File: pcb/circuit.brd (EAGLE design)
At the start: 80 x 70 mm, 148 parts, among them IC1 MCP1612-ADJI/MS, IC2 MCP73833-AMI/UN-ND, IC3 WE-TVS, IC4 MCP3423, IC5 ATWINC1510-MR210PB1952-ND, IC6 MAX3378EEUD, IC7 RN4870, IC8 ATSAML22N18A, J1 22-05-7038-03, J2 22-05-7038-03, Q1 ECX-1210, T1 PMOS, T10 NMOSSOT323, T11 NMOSSOT323, T12 NMOSSOT323, T2 NMOSSOT323, T3 NMOSSOT323, T4 NMOSSOT323, T5 NMOSSOT323, T6 NMOSSOT323, T7 NMOSSOT323, T8 NMOSSOT323, T9 NMOSSOT323, X1 USB2-MICRO, X10 2.5MM-AUDIO-JACK-MONONO_DRILL, X11 2.5MM-AUDIO-JACK-MONONO_DRILL, X12 2.5MM-AUDIO-JACK-MONONO_DRILL, X13 2.5MM-AUDIO-JACK-MONONO_DRILL, X14 MOLEX_1MM_FPC, X15 IGRID-20, X2 B3S-1000, X4 2.5MM-AUDIO-JACK-MONODRILL, X5 2.5MM-AUDIO-JACK-MONODRILL, X6 2.5MM-AUDIO-JACK-MONODRILL, X7 2.5MM-AUDIO-JACK-MONODRILL, X8 2.5MM-AUDIO-JACK-MONODRILL, X9 2.5MM-AUDIO-JACK-MONONO_DRILL

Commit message: routed RN4970
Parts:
- moved R19 31.4 mm to (62.5, 21.8), turned to 90 degrees
- moved C21 31.1 mm to (51.5, 23.6), flipped to the top, turned to 270 degrees
- moved R18 29.6 mm to (60.5, 21.8), turned to 90 degrees
- moved JP6 18.7 mm to (63.1, 35.1), turned to 180 degrees
- moved JP3 17.7 mm to (56.4, 23.4)
- moved R57 14.3 mm to (14.6, 15.2), turned to 0 degrees
- moved JP1 13.9 mm to (60.0, 46.0)
- moved T12 13.6 mm to (14.6, 13.7), turned to 180 degrees
- moved JP7 12.1 mm to (73.0, 51.0)
- moved R23 9.09 mm to (20.3, 39.9)
- moved C27 1.00 mm to (25.1, 43.7)
- moved C30 1.00 mm to (25.1, 45.8)
- moved C32 1.00 mm to (25.1, 47.9)
- moved C34 0.85 mm to (9.34, 27.5)
- moved C13 0.67 mm to (29.2, 31.4), turned to 180 degrees
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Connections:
- net !PG!_TRANS: now also IC6.3; no longer IC6.2
- net BT_MODE: now also IC8.71; no longer IC8.67
- net BT_PAIRING_KEY: now also IC8.67; no longer IC8.71
- net BT_RSSI_IND: now also IC8.70; no longer IC8.68
- net BT_RX_IND: now also IC8.68; no longer IC8.70
- net CHARGER_!PG!: now also IC6.12; no longer IC6.13
- net CHARGER_STAT1: now also IC6.11; no longer IC6.12
- net CHARGER_STAT2: now also IC6.10; no longer IC6.11
- net CHARGER_VUSB_FIL: now also IC6.13; no longer IC6.10
- net OLED_D/C: now also IC8.43; no longer IC8.44
- net OLED_EN: now also IC8.44; no longer IC8.43
- net SENSOR_EN_2: now also IC8.22; no longer IC8.21
- net SENSOR_EN_3: now also IC8.20; no longer IC8.19
- net SENSOR_EN_7: now also IC8.21; no longer IC8.22
- net SENSOR_EN_8: now also IC8.19; no longer IC8.20
- net STAT1_TRANS: now also IC6.4; no longer IC6.3
- net STAT2_TRANS: now also IC6.5; no longer IC6.4
- net USB_CON_INT_TRANS: now also IC6.2; no longer IC6.5
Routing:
- net GND: track 246.0 -> 340.1 mm, vias 6 -> 16
- net BT_UART_TX: track 0.00 -> 71.8 mm, vias 0 -> 2
- net BT_UART_RX: track 0.00 -> 71.3 mm, vias 0 -> 2
- net BT_UART_RTS: track 0.00 -> 55.8 mm, vias 0 -> 4
- net BT_UART_CTS: track 0.00 -> 52.9 mm, vias 0 -> 2
- net !OLED_SPI_CS: track 0.00 -> 49.9 mm, vias 0 -> 1
- net SENSOR_IN_4: track 5.16 -> 51.6 mm, vias 0 -> 1
- net SENSOR_INT_9: track 0.00 -> 44.0 mm, vias 0 -> 2
- net BT_STATUS_1: track 0.00 -> 43.5 mm, vias 0 -> 3
- net SENSOR_IN_7: track 0.21 -> 43.6 mm, vias 0 -> 2
- net BT_STATUS_2: track 0.00 -> 43.0 mm, vias 0 -> 3
- net SENSOR_IN_6: track 5.38 -> 48.4 mm, vias 0 -> 2
- net BT_PAIRING_KEY: track 0.00 -> 42.6 mm, vias 0 -> 1
- net BT_RX_IND: track 0.00 -> 42.0 mm, vias 0 -> 1
- net OLED_SPI_MOSI: track 0.00 -> 41.5 mm
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
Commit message: started routing ATWINC
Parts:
- removed JP2: (no value), thermo:JP4
- added JP8: (no value), thermo:JP3
- moved JP5 58.0 mm to (9.30, 29.9), turned to 180 degrees
- moved R26 7.20 mm to (19.9, 46.0)
- moved R24 6.38 mm to (15.8, 46.0)
- moved R27 4.84 mm to (22.0, 46.0)
- moved JP1 4.06 mm to (56.1, 44.7)
- moved JP4 4.02 mm to (60.6, 38.9)
- moved R25 2.81 mm to (17.9, 46.0)
- moved L5 0.81 mm to (53.9, 32.4)
- moved C25 0.55 mm to (54.5, 29.2)
- moved C29 0.55 mm to (52.5, 29.2)
- moved R28 0.07 mm to (18.2, 39.9)
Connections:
- net !OLED_SPI_CS: now also JP8.3; no longer JP2.3
- net MISO_NC: no longer JP2.4
- net OLED_SPI_MOSI: now also JP8.1; no longer JP2.1
- net OLED_SPI_SCLK: now also JP8.2; no longer JP2.2
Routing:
- net WIFI_SPI_MOSI: track 0.00 -> 54.7 mm, vias 0 -> 2
- net WIFI_SPI_SSN: track 0.00 -> 52.5 mm, vias 0 -> 2
- net WIFI_SPI_MISO: track 0.00 -> 50.4 mm, vias 0 -> 2
- net WIFI_SPI_SCK: track 0.00 -> 48.4 mm, vias 0 -> 2
- net EXT_PWM_0: track 0.00 -> 41.6 mm, vias 0 -> 1
- net EXT_PWM_1: track 0.00 -> 40.6 mm, vias 0 -> 1
- net AGND: track 73.8 -> 102.9 mm
- net RES0: track 0.00 -> 28.1 mm
- net RES1: track 0.00 -> 25.6 mm
- net RES2: track 0.00 -> 22.9 mm
- net WIFI_IRQN: track 0.00 -> 17.7 mm, vias 0 -> 1
- net WIFI_WAKE: track 0.00 -> 15.1 mm, vias 0 -> 1
- net +3V3: track 120.3 -> 135.2 mm
- net OLED_SPI_MOSI: track 41.5 -> 56.1 mm
- net WIFI_SPI_SCK_D: track 0.00 -> 11.4 mm, vias 0 -> 1
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
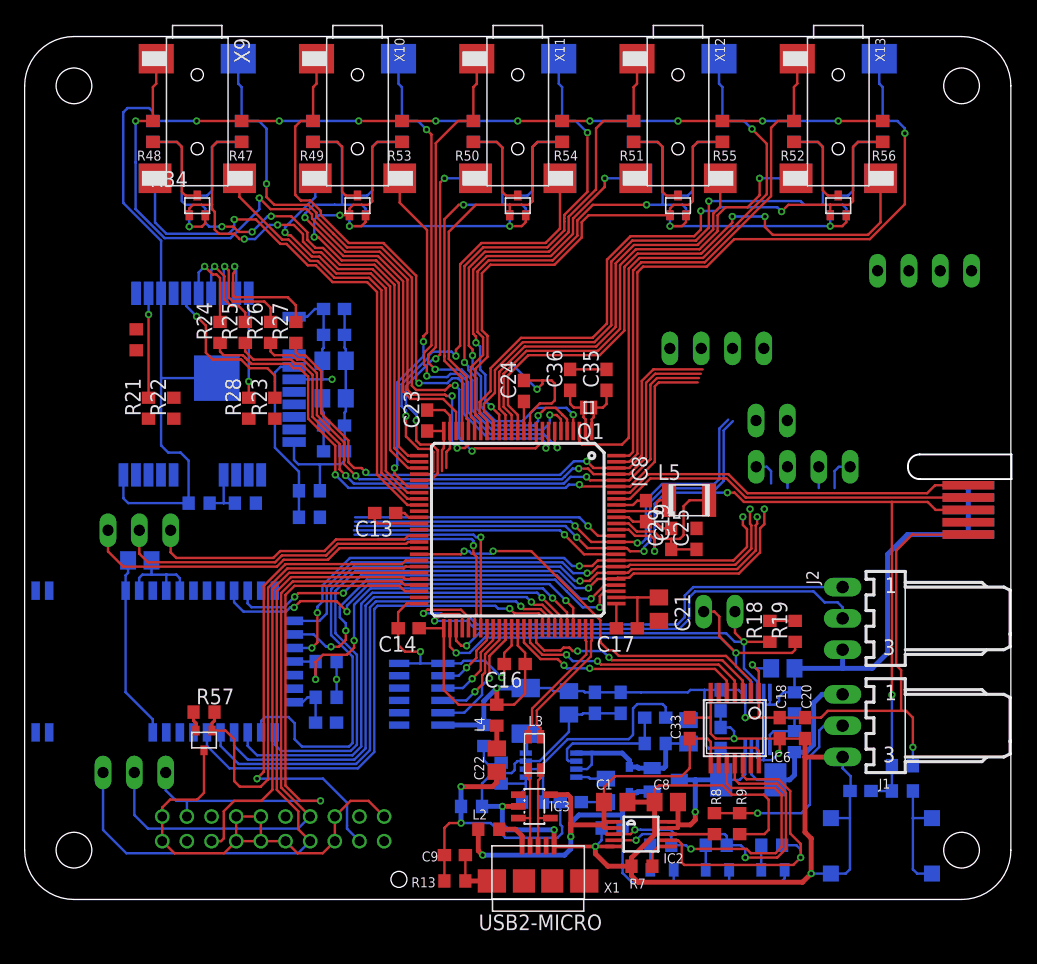
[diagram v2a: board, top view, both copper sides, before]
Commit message: finished routing ATwinc
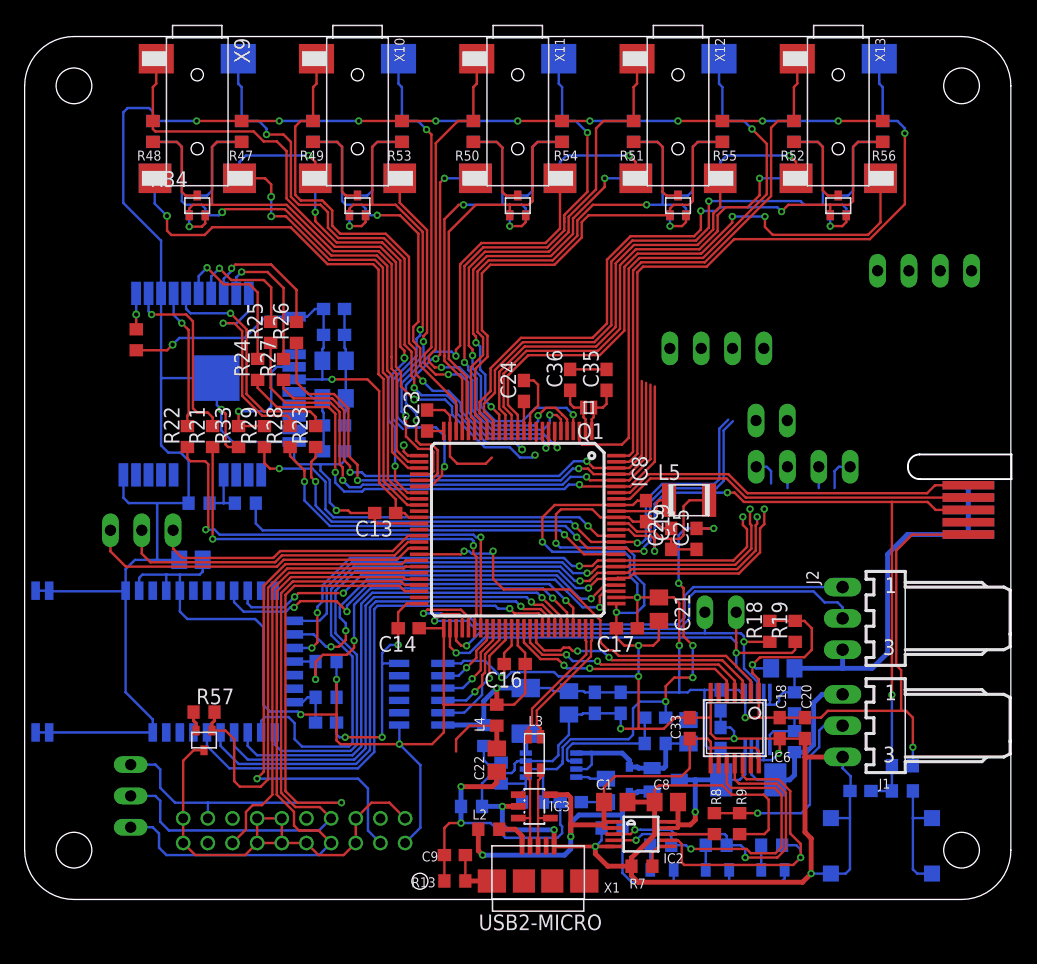
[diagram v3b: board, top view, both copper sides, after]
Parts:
- moved R29 7.50 mm to (19.4, 37.5), flipped to the top, turned to 90 degrees
- moved R33 7.24 mm to (17.4, 37.5), flipped to the top, turned to 90 degrees
- moved R21 5.69 mm to (15.2, 37.5)
- moved R24 4.28 mm to (18.9, 43.0)
- moved C34 4.15 mm to (13.5, 27.6)
- moved R28 4.06 mm to (21.5, 37.5)
- moved R23 4.02 mm to (23.6, 37.5)
- moved R27 3.16 mm to (21.0, 43.0)
- moved R22 2.55 mm to (13.2, 37.5)
- moved R26 2.10 mm to (22.1, 46.0)
- moved R25 2.05 mm to (19.9, 46.0)
- moved JP8 1.92 mm to (8.60, 8.40), turned to 90 degrees
- moved X15 1.71 mm to (21.9, 4.58)
- moved JP5 0.20 mm to (9.50, 29.9)
- moved JP3 0.11 mm to (56.5, 23.3), turned to 90 degrees
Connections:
- net SENSOR_EN_0: now also IC8.28; no longer IC8.27
- net SENSOR_EN_5: now also IC8.27; no longer IC8.28
- net SENSOR_IN_0: now also IC8.10; no longer IC8.9
- net SENSOR_IN_5: now also IC8.9; no longer IC8.10
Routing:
- net +3V3: track 135.2 -> 252.5 mm, vias 6 -> 12
- net GND: track 347.0 -> 453.9 mm, vias 17 -> 26
- net +3V3_ANA: track 8.91 -> 38.1 mm, vias 0 -> 3
- net WIFI_WAKE: track 15.1 -> 35.9 mm, vias 1 -> 2
- net WIFI_IRQN: track 17.7 -> 38.1 mm, vias 1 -> 2
- net WIFI_CHIP_EN: track 21.8 -> 33.6 mm, vias 1 -> 2
- net WIFI_IRQN_D: track 0.12 -> 11.4 mm, vias 0 -> 1
- net WIFI_RESETN: track 22.1 -> 31.9 mm
- net WIFI_UART1_RXD: track 40.3 -> 50.1 mm, vias 2 -> 3
- net SENSOR_IN_5: track 66.2 -> 57.1 mm, vias 4 -> 2
- net WIFI_UART1_TXD: track 39.4 -> 48.2 mm, vias 2 -> 3
- net AGND: track 102.9 -> 94.4 mm, vias 8 -> 12
- net WIFI_SPI_MOSI: track 54.7 -> 46.9 mm
- net WIFI_UART1_RXD_D: track 8.47 -> 16.3 mm
- net !OLED_SPI_CS: track 45.8 -> 52.7 mm
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
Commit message: routing finished
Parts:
- moved JP7 13.5 mm to (63.1, 41.8)
- moved JP4 8.09 mm to (53.6, 42.9)
- moved JP1 3.00 mm to (56.1, 47.7)
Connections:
- net SENSOR_IN_0: now also IC8.9; no longer IC8.10
- net SENSOR_IN_5: now also IC8.10; no longer IC8.9
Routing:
- net +3V3_ANA: track 38.1 -> 270.2 mm, vias 3 -> 12
- net AGND: track 94.4 -> 196.2 mm, vias 12 -> 15
- net GND: track 453.9 -> 512.2 mm, vias 26 -> 33
- net +3V3: track 252.5 -> 278.2 mm, vias 12 -> 14
- net WIFI_SPI_MOSI: track 46.9 -> 61.0 mm
- net WIFI_SPI_SSN: track 48.1 -> 59.9 mm
- net WIFI_SPI_MISO: track 45.0 -> 54.5 mm
- net WIFI_SPI_SCK: track 42.6 -> 49.9 mm
- net BT_UART_RX: track 64.6 -> 71.4 mm
- net BT_UART_TX: track 64.8 -> 71.2 mm
- net BT_UART_CTS: track 46.5 -> 50.7 mm
- net SENSOR_IN_0: track 49.5 -> 53.6 mm
- net BT_UART_RTS: track 48.1 -> 50.3 mm
- net SENSOR_EN_6: track 34.0 -> 35.4 mm
- net CHARGER_VUSB_FIL: track 72.2 -> 73.5 mm
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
